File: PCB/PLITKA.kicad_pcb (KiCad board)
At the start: 2 copper layers, 120.5 x 85.5 mm, 47 parts, among them SW1 SW_DPDT_x2, SW10 MX_SW_HS, SW11 MX_SW_HS, SW12 MX_SW_HS, SW13 MX_SW_HS, SW14 MX_SW_HS, SW15 MX_SW_HS, SW16 MX_SW_HS, SW17 MX_SW_HS, SW18 MX_SW_HS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

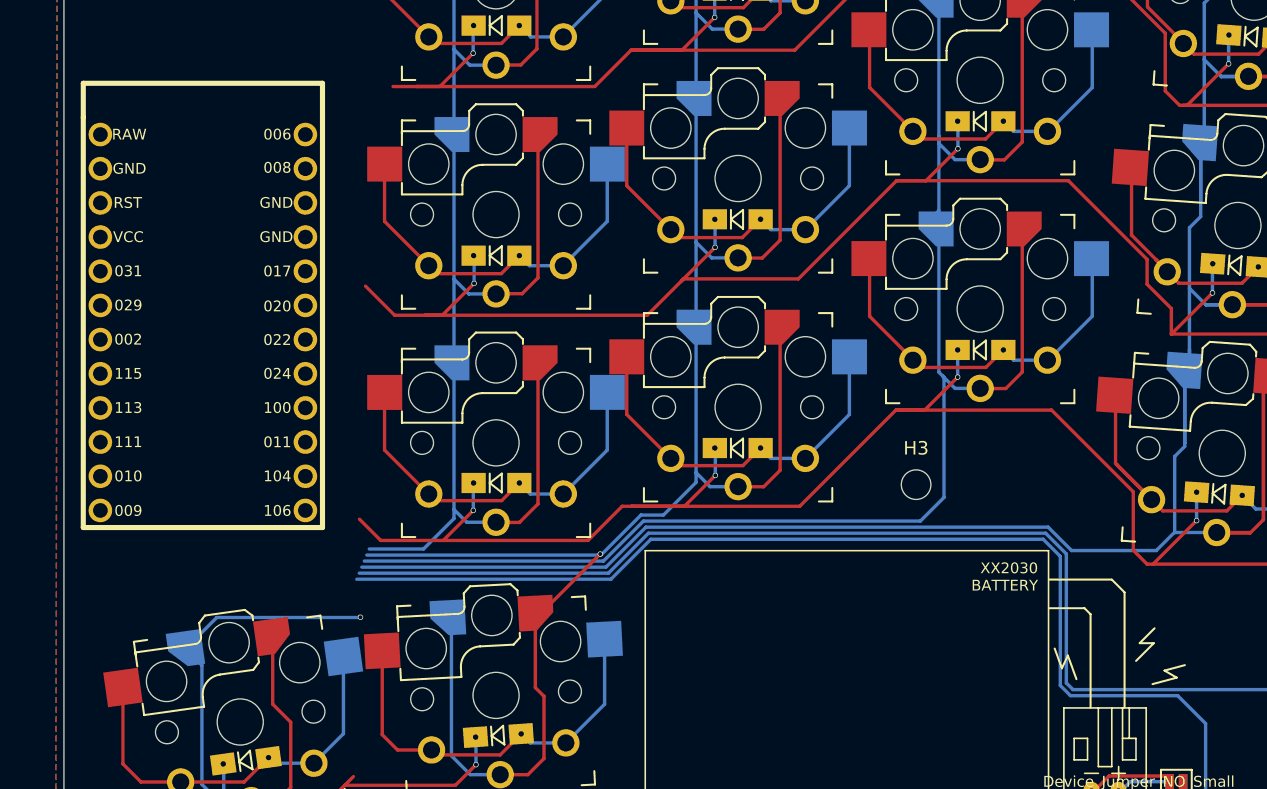
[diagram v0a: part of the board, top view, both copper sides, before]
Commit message: Rudimentary silkscreen clean up
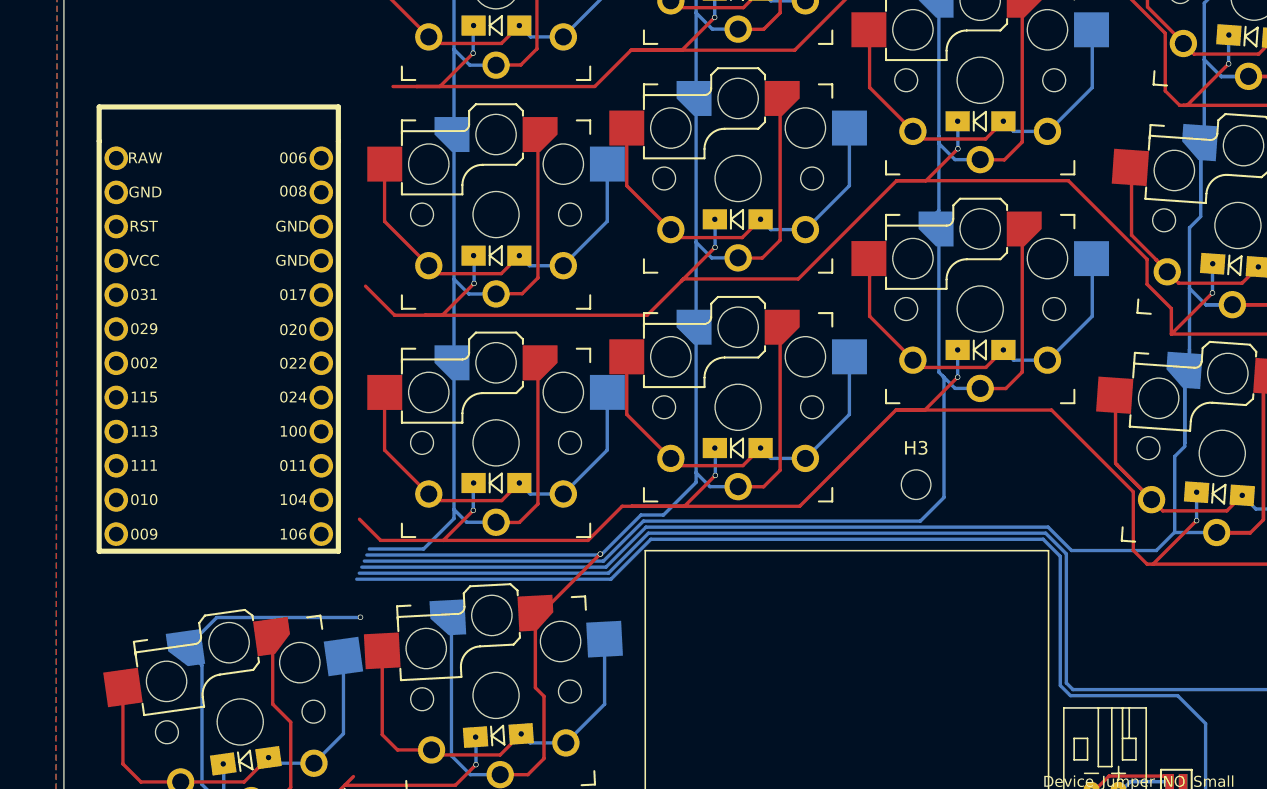
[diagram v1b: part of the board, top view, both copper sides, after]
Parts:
- moved U1 2.12 mm to (98.3, 93.1)
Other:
- board text removed: "XX2030 BATTERY"

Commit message: Fix: replace SW1 DPDT symbol with SPDT to match the footprint
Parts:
- SW1: value SW_DPDT_x2 -> SW_SPDT_321
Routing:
- net unconnected-(SW1A-A-Pad1)_1: track 2.55 -> 0.00 mm
- net unconnected-(SW1-C-Pad1)_1: track 0.00 -> 2.55 mm
